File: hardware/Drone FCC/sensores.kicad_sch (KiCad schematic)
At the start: 12 parts, among them J201 Mag Dupont, J202 Mag DF13, J203 GPS Dupont, J204 GPS M8N - DF13, U201 ICM-42688-V, U202 ILPS22QSTR

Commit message: positioned components in 100x60 board with incomplete routing
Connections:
- net GND: now also J203.6 (Pin_6); no longer J203.3 (Pin_3)
- net GNSS_PPS: now also J203.2 (Pin_2), J204.4; no longer J203.6 (Pin_6)
- net GNSS_Rx: now also J203.1 (Pin_1); no longer J203.2 (Pin_2)
- net GNSS_SCL: no longer J204.4
- net GNSS_SDA: no longer J204.5
- net GNSS_Tx: now also J203.3 (Pin_3); no longer J203.1 (Pin_1)
- net MAG_SDA: now also J201.3 (Pin_3); no longer J201.6 (Pin_6)
- no-connect marks 4 -> 5
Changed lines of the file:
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@@
   (no_connect (at 100.965 34.925))
   (no_connect (at 100.965 40.005))
-  (no_connect (at 15.24 189.23))
+  (no_connect (at 149.225 172.085))
   (no_connect (at 100.965 37.465))
-  (wire (pts (xy 113.03 147.955) (xy 125.73 147.955))
+  (no_connect (at 53.34 191.77))
+  (wire (pts (xy 113.03 153.035) (xy 125.73 153.035))
     (stroke (width 0) (type default) (color 0 0 0 0))
   )
@@
     (stroke (width 1) (type default) (color 0 0 0 0))
   )
-  (wire (pts (xy 45.085 191.77) (xy 54.61 191.77))
+  (wire (pts (xy 32.385 189.23) (xy 22.86 189.23))
     (stroke (width 0) (type default) (color 0 0 0 0))
   )
@@
     (stroke (width 1) (type default) (color 0 0 0 0))
   )
-  (wire (pts (xy 113.03 153.035) (xy 113.03 153.67))
-    (stroke (width 0) (type default) (color 0 0 0 0))
-  )
   (wire (pts (xy 121.285 22.225) (xy 121.285 24.765))
     (stroke (width 0) (type default) (color 0 0 0 0))
@@
     (stroke (width 0) (type default) (color 0 0 0 0))
   )
+  (wire (pts (xy 175.895 162.56) (xy 191.135 162.56))
+    (stroke (width 0) (type default) (color 0 0 0 0))
+  )
   (wire (pts (xy 132.715 28.575) (xy 132.715 32.385))
     (stroke (width 0) (type default) (color 0 0 0 0))
@@
     (stroke (width 0) (type default) (color 0 0 0 0))
   )
+  (wire (pts (xy 138.43 150.495) (xy 148.59 150.495))
+    (stroke (width 0) (type default) (color 0 0 0 0))
+  )
   (wire (pts (xy 137.16 172.085) (xy 149.225 172.085))
     (stroke (width 0) (type default) (color 0 0 0 0))
@@
     (stroke (width 0) (type default) (color 0 0 0 0))
   )
+  (wire (pts (xy 45.085 191.77) (xy 53.34 191.77))
+    (stroke (width 0) (type default) (color 0 0 0 0))
+  )
   (wire (pts (xy 107.95 100.33) (xy 101.6 100.33))
     (stroke (width 0) (type default) (color 0 0 0 0))
@@
     (stroke (width 0) (type default) (color 0 0 0 0))
   )
-  (wire (pts (xy 15.24 189.23) (xy 32.385 189.23))
-    (stroke (width 0) (type default) (color 0 0 0 0))
-  )
   (wire (pts (xy 107.95 97.79) (xy 107.95 100.33))
     (stroke (width 0) (type default) (color 0 0 0 0))
   )
-  (wire (pts (xy 138.43 147.955) (xy 142.875 147.955))
+  (wire (pts (xy 113.03 150.495) (xy 125.73 150.495))
     (stroke (width 0) (type default) (color 0 0 0 0))
   )
@@
     (stroke (width 0) (type default) (color 0 0 0 0))
   )
+  (wire (pts (xy 158.115 147.955) (xy 158.115 149.86))
+    (stroke (width 0) (type default) (color 0 0 0 0))
+  )
   (wire (pts (xy 34.29 42.545) (xy 45.085 42.545))
     (stroke (width 0) (type default) (color 0 0 0 0))
@@
     (stroke (width 1) (type default) (color 0 0 0 0))
   )
-  (wire (pts (xy 113.03 150.495) (xy 125.73 150.495))
+  (wire (pts (xy 113.03 147.955) (xy 125.73 147.955))
     (stroke (width 0) (type default) (color 0 0 0 0))
   )
@@
     (stroke (width 0) (type default) (color 0 0 0 0))
   )
-  (wire (pts (xy 113.03 153.035) (xy 125.73 153.035))
+  (wire (pts (xy 138.43 147.955) (xy 158.115 147.955))
     (stroke (width 0) (type default) (color 0 0 0 0))
   )
   (wire (pts (xy 138.43 153.035) (xy 142.875 153.035))
-    (stroke (width 0) (type default) (color 0 0 0 0))
-  )
-  (wire (pts (xy 138.43 150.495) (xy 153.67 150.495))
     (stroke (width 0) (type default) (color 0 0 0 0))
   )
@@
     (effects (font (size 2.54 2.54)) (justify left bottom))
   )
+  (label "GNSS_PPS" (at 175.895 162.56 0)
+    (effects (font (size 1.27 1.27)) (justify left bottom))
+  )
   (label "GNSS_Rx" (at 149.225 177.165 180)
     (effects (font (size 1.27 1.27)) (justify right bottom))
@@
     (effects (font (size 1.27 1.27)) (justify right bottom))
   )
-  (label "GNSS_Rx" (at 113.03 150.495 0)
+  (label "GNSS_Rx" (at 113.03 147.955 0)
     (effects (font (size 1.27 1.27)) (justify left bottom))
   )
@@
     (effects (font (size 1.27 1.27)) (justify right bottom))
   )
-  (label "GNSS_Tx" (at 113.03 147.955 0)
-    (effects (font (size 1.27 1.27)) (justify left bottom))
+  (label "GNSS_Tx" (at 113.03 153.035 0)
+    (effects (font (size 1.27 1.27)) (justify left bottom))
+  )
+  (label "GNSS_PPS" (at 149.225 174.625 180)
+    (effects (font (size 1.27 1.27)) (justify right bottom))
   )
   (label "GNSS_Tx" (at 149.225 179.705 180)
     (effects (font (size 1.27 1.27)) (justify right bottom))
   )
-  (label "GNSS_SCL" (at 149.225 174.625 180)
-    (effects (font (size 1.27 1.27)) (justify right bottom))
+  (label "GNSS_PPS" (at 113.03 150.495 0)
+    (effects (font (size 1.27 1.27)) (justify left bottom))
   )
   (label "MAG_SDA" (at 33.655 165.735 180)
@@
     (effects (font (size 1.27 1.27)) (justify right bottom))
   )
-  (label "MAG_SDA" (at 54.61 191.77 180)
-    (effects (font (size 1.27 1.27)) (justify right bottom))
-  )
-  (label "GNSS_SDA" (at 149.225 172.085 180)
-    (effects (font (size 1.27 1.27)) (justify right bottom))
+  (label "MAG_SDA" (at 22.86 189.23 0)
+    (effects (font (size 1.27 1.27)) (justify left bottom))
   )
   (global_label "5V" (shape input) (at 151.13 182.245 0) (fields_autoplaced)
@@
     )
   )
-  (global_label "5V" (shape input) (at 153.67 150.495 0) (fields_autoplaced)
-    (effects (font (size 1.27 1.27)) (justify left))
-    (property "Intersheet References" "${INTERSHEET_REFS}" (id 0) (at 158.3812 150.4156 0)
+  (global_label "5V" (shape input) (at 148.59 150.495 0) (fields_autoplaced)
+    (effects (font (size 1.27 1.27)) (justify left))
+    (property "Intersheet References" "${INTERSHEET_REFS}" (id 0) (at 153.3012 150.4156 0)
       (effects (font (size 1.27 1.27)) (justify left) hide)
     )
@@
     )
   )
+  (hierarchical_label "GNSS_PPS" (shape output) (at 191.135 162.56 0)
+    (effects (font (size 1.27 1.27)) (justify left))
+  )
   (hierarchical_label "IMU_CS" (shape input) (at 34.925 34.925 180)
     (effects (font (size 1.27 1.27)) (justify right))
@@
   (hierarchical_label "IMU_CLK" (shape input) (at 34.925 37.465 180)
     (effects (font (size 1.27 1.27)) (justify right))
-  )
-  (hierarchical_label "GNSS_PPS" (shape output) (at 142.875 147.955 0)
-    (effects (font (size 1.27 1.27)) (justify left))
   )
   (hierarchical_label "BARO_SDA" (shape bidirectional) (at 26.67 100.33 180)
@@
     (pin "MP")
   )
-  (symbol (lib_id "power:GND") (at 113.03 153.67 0) (unit 1)
+  (symbol (lib_id "power:GND") (at 158.115 149.86 0) (mirror y) (unit 1)
     (in_bom yes) (on_board yes)
-    (property "Reference" "#PWR0110" (id 0) (at 113.03 160.02 0)
-      (effects (font (size 1.27 1.27)) hide)
-    )
-    (property "Value" "GND" (id 1) (at 113.03 158.75 0))
-    (property "Footprint" "" (id 2) (at 113.03 153.67 0)
-      (effects (font (size 1.27 1.27)) hide)
-    )
-    (property "Datasheet" "" (id 3) (at 113.03 153.67 0)
-      (effects (font (size 1.27 1.27)) hide)
-    )
+    (property "Reference" "#PWR0110" (id 0) (at 158.115 156.21 0)
+      (effects (font (size 1.27 1.27)) hide)
+    )
+    (property "Value" "GND" (id 1) (at 158.115 154.94 0))
+    (property "Footprint" "" (id 2) (at 158.115 149.86 0)
+      (effects (font (size 1.27 1.27)) hide)
+    )
+    (property "Datasheet" "" (id 3) (at 158.115 149.86 0)
+      (effects (font (size 1.27 1.27)) hide)
+    )

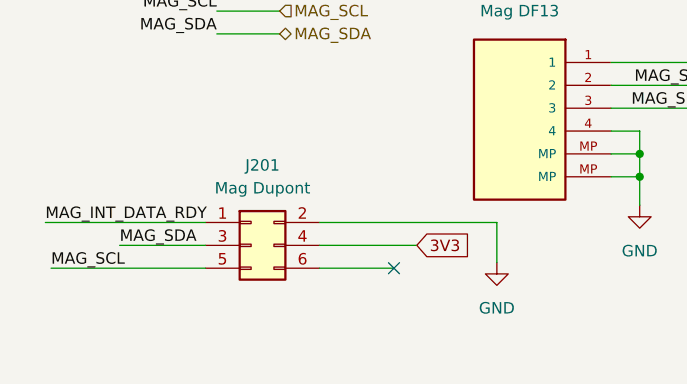
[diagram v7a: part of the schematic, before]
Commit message: todo: route SWD connector
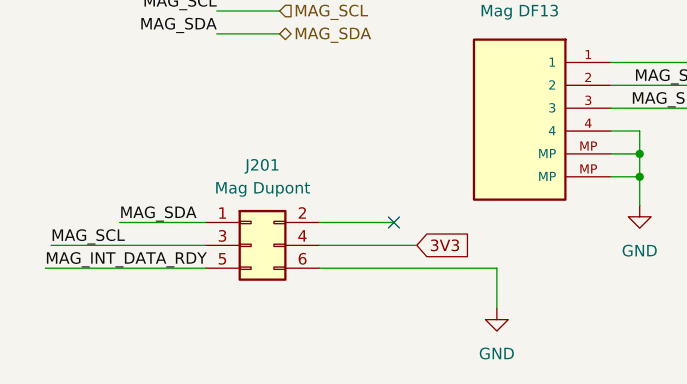
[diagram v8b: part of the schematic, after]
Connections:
- net GND: now also J201.6 (Pin_6); no longer J201.2 (Pin_2)
- net MAG_INT_DATA_RDY: now also J201.5 (Pin_5); no longer J201.1 (Pin_1)
- net MAG_SCL: now also J201.3 (Pin_3); no longer J201.5 (Pin_5)
- net MAG_SDA: now also J201.1 (Pin_1); no longer J201.3 (Pin_3)
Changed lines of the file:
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@@
   (no_connect (at 149.225 172.085))
   (no_connect (at 100.965 37.465))
-  (no_connect (at 53.34 191.77))
+  (no_connect (at 53.34 186.69))
   (wire (pts (xy 113.03 153.035) (xy 125.73 153.035))
     (stroke (width 0) (type default) (color 0 0 0 0))
@@
     (stroke (width 1) (type default) (color 0 0 0 0))
   )
-  (wire (pts (xy 32.385 189.23) (xy 22.86 189.23))
+  (wire (pts (xy 32.385 186.69) (xy 22.86 186.69))
     (stroke (width 0) (type default) (color 0 0 0 0))
   )
@@
     (stroke (width 0) (type default) (color 0 0 0 0))
   )
-  (wire (pts (xy 14.605 186.69) (xy 32.385 186.69))
+  (wire (pts (xy 14.605 191.77) (xy 32.385 191.77))
     (stroke (width 0) (type default) (color 0 0 0 0))
   )
@@
     (stroke (width 0) (type default) (color 0 0 0 0))
   )
-  (wire (pts (xy 64.77 186.69) (xy 64.77 191.135))
+  (wire (pts (xy 64.77 191.77) (xy 64.77 196.215))
     (stroke (width 0) (type default) (color 0 0 0 0))
   )
@@
     (stroke (width 0) (type default) (color 0 0 0 0))
   )
-  (wire (pts (xy 45.085 191.77) (xy 53.34 191.77))
+  (wire (pts (xy 53.34 186.69) (xy 45.085 186.69))
     (stroke (width 0) (type default) (color 0 0 0 0))
   )
@@
     (stroke (width 0) (type default) (color 0 0 0 0))
   )
-  (wire (pts (xy 15.24 191.77) (xy 32.385 191.77))
+  (wire (pts (xy 15.24 189.23) (xy 32.385 189.23))
     (stroke (width 0) (type default) (color 0 0 0 0))
   )
@@
     (stroke (width 0) (type default) (color 0 0 0 0))
   )
-  (wire (pts (xy 45.085 186.69) (xy 64.77 186.69))
+  (wire (pts (xy 45.085 191.77) (xy 64.77 191.77))
     (stroke (width 0) (type default) (color 0 0 0 0))
   )
@@
     (effects (font (size 1.27 1.27)) (justify right bottom))
   )
-  (label "MAG_SCL" (at 15.24 191.77 0)
+  (label "MAG_SCL" (at 15.24 189.23 0)
     (effects (font (size 1.27 1.27)) (justify left bottom))
   )
@@
     (effects (font (size 1.27 1.27)) (justify left bottom))
   )
-  (label "MAG_INT_DATA_RDY" (at 14.605 186.69 0)
+  (label "MAG_INT_DATA_RDY" (at 14.605 191.77 0)
     (effects (font (size 1.27 1.27)) (justify left bottom))
   )
@@
     (effects (font (size 1.27 1.27)) (justify right bottom))
   )
-  (label "MAG_SDA" (at 22.86 189.23 0)
+  (label "MAG_SDA" (at 22.86 186.69 0)
     (effects (font (size 1.27 1.27)) (justify left bottom))
   )
@@
     (pin "2")
   )
-  (symbol (lib_id "power:GND") (at 64.77 191.135 0) (unit 1)
-    (in_bom yes) (on_board yes) (fields_autoplaced)
-    (property "Reference" "#PWR0107" (id 0) (at 64.77 197.485 0)
-      (effects (font (size 1.27 1.27)) hide)
-    )
-    (property "Value" "GND" (id 1) (at 64.77 196.215 0))
-    (property "Footprint" "" (id 2) (at 64.77 191.135 0)
-      (effects (font (size 1.27 1.27)) hide)
-    )
-    (property "Datasheet" "" (id 3) (at 64.77 191.135 0)
-      (effects (font (size 1.27 1.27)) hide)
-    )
+  (symbol (lib_id "power:GND") (at 64.77 196.215 0) (unit 1)
+    (in_bom yes) (on_board yes) (fields_autoplaced)
+    (property "Reference" "#PWR0107" (id 0) (at 64.77 202.565 0)
+      (effects (font (size 1.27 1.27)) hide)
+    )
+    (property "Value" "GND" (id 1) (at 64.77 201.295 0))
+    (property "Footprint" "" (id 2) (at 64.77 196.215 0)
+      (effects (font (size 1.27 1.27)) hide)
+    )
+    (property "Datasheet" "" (id 3) (at 64.77 196.215 0)
+      (effects (font (size 1.27 1.27)) hide)
+    )
